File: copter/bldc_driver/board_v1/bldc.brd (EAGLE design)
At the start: 41.5 x 54.5 mm, 90 parts, among them IC1 LM339APWR, IC2 7411, IC3 7411, IC4 CD4051BPWR, IC5 FAN7388, Y1 16MHz

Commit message: simple arduino makefile
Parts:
- C10, C15: value 100nF -> 10nF
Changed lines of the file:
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@@
 <attribute name="PROD_ID" value="CAP-00867" x="32.5" y="13.5" size="1.778" layer="27" rot="R270" display="off"/>
 </element>
-<element name="C10" library="SparkFun-Capacitors" package="0402-CAP" value="100nF" x="37.381" y="33.3048" rot="R180">
+<element name="C10" library="SparkFun-Capacitors" package="0402-CAP" value="10nF" x="37.381" y="33.3048" rot="R180">
 <attribute name="PROD_ID" value="CAP-00867" x="37.381" y="33.3048" size="1.778" layer="27" rot="R180" display="off"/>
 </element>
@@
 <element name="LWL" library="kmod" package="0603_LED" value="" x="25" y="19.5"/>
 <element name="IC1" library="kmod" package="TSSOP14" value="LM339APWR" x="8.5" y="24.5"/>
-<element name="C15" library="SparkFun-Capacitors" package="0402-CAP" value="100nF" x="8" y="19.5" rot="R90">
+<element name="C15" library="SparkFun-Capacitors" package="0402-CAP" value="10nF" x="8" y="19.5" rot="R90">
 <attribute name="PROD_ID" value="CAP-00867" x="8" y="19.5" size="1.778" layer="27" rot="R90" display="off"/>
 </element>

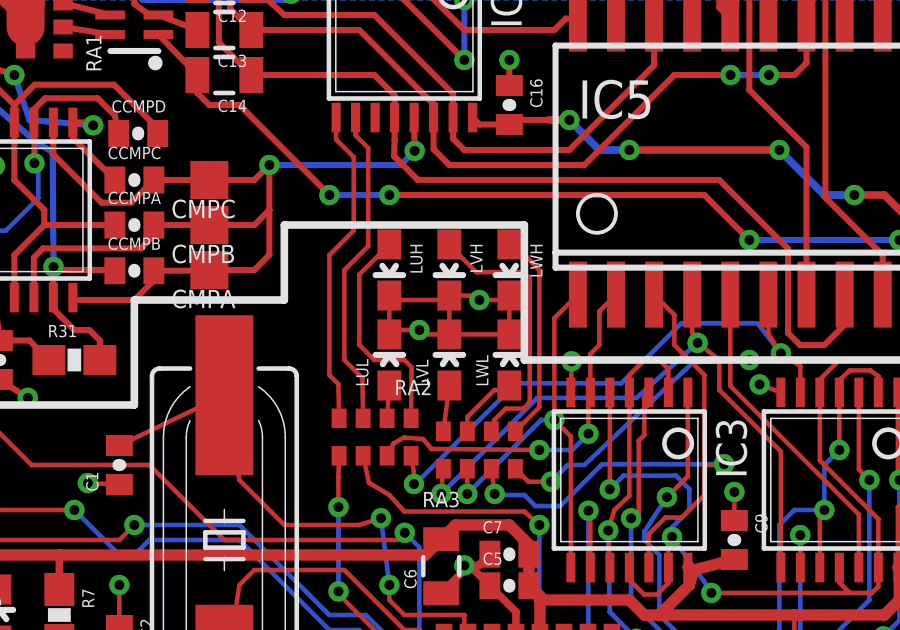
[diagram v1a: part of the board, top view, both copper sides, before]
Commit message: fix some of the names in the bldc eagle files; update driver firmware to work with new board
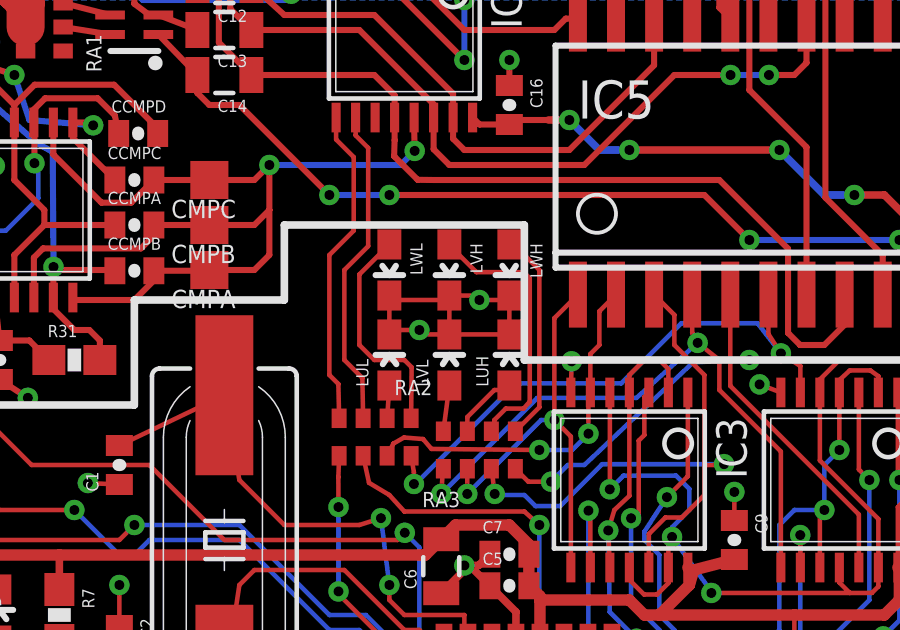
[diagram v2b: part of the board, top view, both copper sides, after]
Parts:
- moved LUH 5.00 mm to (25.0, 19.5), turned to 0 degrees
- moved LWL 5.00 mm to (21.0, 22.5), turned to 180 degrees
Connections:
- net N$8: now also LUH.A; no longer LWL.A
- net N$9: now also LWL.A; no longer LUH.A
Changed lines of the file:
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@@
 <setting verticaltext="up"/>
 </settings>
-<grid distance="0.5" unitdist="mm" unit="mm" style="lines" multiple="1" display="yes" altdistance="1" altunitdist="mil" altunit="mil"/>
+<grid distance="0.5" unitdist="mm" unit="mm" style="lines" multiple="1" display="yes" altdistance="0.01" altunitdist="mm" altunit="mm"/>
 <layers>
 <layer number="1" name="Top" color="4" fill="1" visible="yes" active="yes"/>
@@
 <attribute name="VOLTAGE" value="40" x="15.5" y="29" size="1.778" layer="27" rot="R180" display="off"/>
 </element>
-<element name="LUH" library="kmod" package="0603_LED" value="" x="21" y="22.5" rot="R180"/>
+<element name="LWL" library="kmod" package="0603_LED" value="" x="21" y="22.5" rot="R180"/>
 <element name="LVH" library="kmod" package="0603_LED" value="" x="23" y="22.5" rot="R180"/>
 <element name="LWH" library="kmod" package="0603_LED" value="" x="25" y="22.5" rot="R180"/>
 <element name="LUL" library="kmod" package="0603_LED" value="" x="21" y="19.5"/>
 <element name="LVL" library="kmod" package="0603_LED" value="" x="23" y="19.5"/>
-<element name="LWL" library="kmod" package="0603_LED" value="" x="25" y="19.5"/>
+<element name="LUH" library="kmod" package="0603_LED" value="" x="25" y="19.5"/>
 <element name="IC1" library="kmod" package="TSSOP14" value="LM339APWR" x="8.5" y="24.5"/>
 <element name="C15" library="SparkFun-Capacitors" package="0402-CAP" value="10nF" x="8" y="19.5" rot="R90">
@@
 <wire x1="3" y1="26.5" x2="2.4" y2="27.1" width="0.2032" layer="1"/>
 <wire x1="2.4" y1="27.1" x2="2.4" y2="27.375" width="0.2032" layer="1"/>
+<contactref element="LUH" pad="C"/>
 <contactref element="LWL" pad="C"/>
-<contactref element="LUH" pad="C"/>
 <wire x1="25" y1="21.6484" x2="24.8516" y2="21.5" width="0.1524" layer="1"/>
 <wire x1="24.8516" y1="21.5" x2="24" y2="21.5" width="0.1524" layer="1"/>
@@
 </signal>
 <signal name="N$8">
-<contactref element="LWL" pad="A"/>
+<contactref element="LUH" pad="A"/>
 <contactref element="RA3" pad="7"/>
 <wire x1="25" y1="18.6484" x2="24.8516" y2="18.5" width="0.1524" layer="1"/>
@@
 </signal>
 <signal name="N$9">
-<contactref element="LUH" pad="A"/>
+<contactref element="LWL" pad="A"/>
 <contactref element="RA2" pad="1"/>
 <wire x1="21" y1="23.3516" x2="20" y2="22.3516" width="0.1524" layer="1"/>

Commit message: changed some of the bldc board values
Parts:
- C10, C15: value 10nF -> 10nF 50V
- C11, C12, C13, C14: value 4.7uF -> 4.7uF 50V
- C22: value 100nF -> 10nF 50V
- C25: value 100uF -> 100uF 50V
- C3: value 1mF -> 1mF 50V
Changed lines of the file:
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@@
 <attribute name="PROD_ID" value="CAP-00867" x="32.5" y="13.5" size="1.778" layer="27" rot="R270" display="off"/>
 </element>
-<element name="C10" library="SparkFun-Capacitors" package="0402-CAP" value="10nF" x="37.381" y="33.3048" rot="R180">
+<element name="C10" library="SparkFun-Capacitors" package="0402-CAP" value="10nF 50V" x="37.381" y="33.3048" rot="R180">
 <attribute name="PROD_ID" value="CAP-00867" x="37.381" y="33.3048" size="1.778" layer="27" rot="R180" display="off"/>
 </element>
-<element name="C11" library="SparkFun-Capacitors" package="0805" value="4.7uF" x="37.4318" y="34.627" rot="R180">
+<element name="C11" library="SparkFun-Capacitors" package="0805" value="4.7uF 50V" x="37.4318" y="34.627" rot="R180">
 <attribute name="PROD_ID" value="CAP-08402" x="37.4318" y="34.627" size="1.778" layer="27" rot="R180" display="off"/>
 </element>
-<element name="C12" library="SparkFun-Capacitors" package="0805" value="4.7uF" x="15.5" y="32" rot="R180">
+<element name="C12" library="SparkFun-Capacitors" package="0805" value="4.7uF 50V" x="15.5" y="32" rot="R180">
 <attribute name="PROD_ID" value="CAP-08402" x="15.5" y="32" size="1.778" layer="27" rot="R180" display="off"/>
 <attribute name="VOLTAGE" value="40" x="15.5" y="32" size="1.778" layer="27" rot="R180" display="off"/>
 </element>
-<element name="C13" library="SparkFun-Capacitors" package="0805" value="4.7uF" x="15.5" y="30.5" rot="R180">
+<element name="C13" library="SparkFun-Capacitors" package="0805" value="4.7uF 50V" x="15.5" y="30.5" rot="R180">
 <attribute name="PROD_ID" value="CAP-08402" x="15.5" y="30.5" size="1.778" layer="27" rot="R180" display="off"/>
 <attribute name="VOLTAGE" value="40" x="15.5" y="30.5" size="1.778" layer="27" rot="R180" display="off"/>
 </element>
-<element name="C14" library="SparkFun-Capacitors" package="0805" value="4.7uF" x="15.5" y="29" rot="R180">
+<element name="C14" library="SparkFun-Capacitors" package="0805" value="4.7uF 50V" x="15.5" y="29" rot="R180">
 <attribute name="PROD_ID" value="CAP-08402" x="15.5" y="29" size="1.778" layer="27" rot="R180" display="off"/>
 <attribute name="VOLTAGE" value="40" x="15.5" y="29" size="1.778" layer="27" rot="R180" display="off"/>
@@
 <element name="LUH" library="kmod" package="0603_LED" value="" x="25" y="19.5"/>
 <element name="IC1" library="kmod" package="TSSOP14" value="LM339APWR" x="8.5" y="24.5"/>
-<element name="C15" library="SparkFun-Capacitors" package="0402-CAP" value="10nF" x="8" y="19.5" rot="R90">
+<element name="C15" library="SparkFun-Capacitors" package="0402-CAP" value="10nF 50V" x="8" y="19.5" rot="R90">
 <attribute name="PROD_ID" value="CAP-00867" x="8" y="19.5" size="1.778" layer="27" rot="R90" display="off"/>
 </element>
@@
 <attribute name="PROD_ID" value="CAP-00867" x="12.5" y="25.5" size="1.778" layer="27" display="off"/>
 </element>
-<element name="C22" library="SparkFun-Capacitors" package="0402-CAP" value="100nF" x="40" y="45" rot="R90">
+<element name="C22" library="SparkFun-Capacitors" package="0402-CAP" value="10nF 50V" x="40" y="45" rot="R90">
 <attribute name="PROD_ID" value="CAP-00867" x="40" y="45" size="1.778" layer="27" rot="R90" display="off"/>
 </element>
@@
 <element name="QWH" library="kmod" package="POWERSO8" value="" x="28" y="50.5"/>
 <element name="DARR1" library="kmod" package="SOT363" value="" x="12.5" y="31" rot="R90"/>
-<element name="C3" library="kmod" package="CPOL-RADIAL-1000UF-50V" value="1mF" x="40" y="45" rot="R90"/>
-<element name="C25" library="kmod" package="CPOL-RADIAL-100UF-25V" value="100uF" x="40" y="34.5" rot="R90"/>
+<element name="C3" library="kmod" package="CPOL-RADIAL-1000UF-50V" value="1mF 50V" x="40" y="45" rot="R90"/>
+<element name="C25" library="kmod" package="CPOL-RADIAL-100UF-25V" value="100uF 50V" x="40" y="34.5" rot="R90"/>
 <element name="CONN_BATT" library="kmod" package="HOLE_18AWG" value="" x="8" y="52" rot="R180"/>
 <element name="CONN_BATT_GND" library="kmod" package="HOLE_18AWG" value="" x="1.5" y="33.5" rot="R180"/>

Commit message: update values based on board #1
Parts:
- LD1: value (none) -> WHT
- LD13: value (none) -> BLUE
- LP5V: value (none) -> YELLOW
- LPBAT: value (none) -> GRN
- R6: value 470 -> 1k
- RA9: value 1k -> 2.2k
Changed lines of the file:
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@@
 <element name="U$3" library="SparkFun-Electromechanical" package="STAND-OFF" value="" x="38" y="3"/>
 <element name="U$4" library="SparkFun-Electromechanical" package="STAND-OFF" value="" x="3" y="3"/>
-<element name="R6" library="SparkFun-Resistors" package="0603-RES" value="470" x="17.5" y="2" rot="R90"/>
-<element name="LD13" library="kmod" package="0603_LED" value="" x="16" y="2" rot="R180"/>
+<element name="R6" library="SparkFun-Resistors" package="0603-RES" value="1k" x="17.5" y="2" rot="R90"/>
+<element name="LD13" library="kmod" package="0603_LED" value="BLUE" x="16" y="2" rot="R180"/>
 <element name="R7" library="SparkFun-Resistors" package="0603-RES" value="470" x="10" y="11" rot="R270"/>
-<element name="LP5V" library="kmod" package="0603_LED" value="" x="8" y="11"/>
-<element name="LPBAT" library="kmod" package="0603_LED" value="" x="1.5" y="39"/>
+<element name="LP5V" library="kmod" package="0603_LED" value="YELLOW" x="8" y="11"/>
+<element name="LPBAT" library="kmod" package="0603_LED" value="GRN" x="1.5" y="39"/>
 <element name="C5" library="SparkFun-Capacitors" package="0402-CAP" value="100nF" x="25" y="11.9746">
 <attribute name="PROD_ID" value="CAP-00867" x="25" y="11.9746" size="1.778" layer="27" display="off"/>
@@
 <element name="PAD11" library="kmod" package="TESTPAD" value="PD1" x="32" y="9" rot="R180"/>
 <element name="PAD12" library="kmod" package="TESTPAD" value="VREF" x="4.5" y="22.5" rot="R270"/>
-<element name="LD1" library="kmod" package="0603_LED" value="" x="2.5" y="39"/>
-<element name="RA9" library="kmod" package="0603-ARV" value="1k" x="2" y="42" rot="R180"/>
+<element name="LD1" library="kmod" package="0603_LED" value="WHT" x="2.5" y="39"/>
+<element name="RA9" library="kmod" package="0603-ARV" value="2.2k" x="2" y="42" rot="R180"/>
 </elements>
 <signals>

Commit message: got the board somewhat working, though it has trouble driving the new motors
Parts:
- R31, R32: value 22k -> 220k
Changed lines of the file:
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@@
 </element>
 <element name="IC4" library="kmod" package="TSSOP16" value="CD4051BPWR" x="21.5" y="30.5" rot="R180"/>
-<element name="R31" library="SparkFun-Resistors" package="0603-RES" value="22k" x="10.5" y="19.5"/>
-<element name="R32" library="SparkFun-Resistors" package="0603-RES" value="22k" x="4.5" y="28" rot="R270"/>
+<element name="R31" library="SparkFun-Resistors" package="0603-RES" value="220k" x="10.5" y="19.5"/>
+<element name="R32" library="SparkFun-Resistors" package="0603-RES" value="220k" x="4.5" y="28" rot="R270"/>
 <element name="CCMPB" library="SparkFun-Capacitors" package="0402-CAP" value="10pF" x="12.5" y="22.4746">
 <attribute name="PROD_ID" value="CAP-00867" x="12.5" y="22.4746" size="1.778" layer="27" display="off"/>
